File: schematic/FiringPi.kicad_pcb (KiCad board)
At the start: 4 copper layers, 65 x 85.9 mm, 72 parts, among them IC1 HX711, J12 UART, P1 Raspberry Pi GPIO Header, Q1 MMBT4403, U4 LM2596S-5, U5 ADS1115IDGS, U6 MAX31865xAP, U7 MAX31865xAP

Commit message: Updated silkscreen labels
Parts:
- renumbered RELAY1 to RELAY, J12 to UART
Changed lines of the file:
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@@
     (property "Sheetname" "")
     (attr through_hole)
-    (fp_text reference "J12" (at 9.5 -0.025 270 unlocked) (layer "F.SilkS")
+    (fp_text reference "UART" (at 9.5 -0.025 270 unlocked) (layer "F.SilkS")
       (effects (font (size 1 1) (thickness 0.15)))
     )
@@
     (property "Sheetname" "")
     (attr through_hole)
-    (fp_text reference "RELAY1" (at 3 11.425) (layer "F.SilkS")
-      (effects (font (size 1 1) (thickness 0.15)))
-    )
+    (fp_text reference "RELAY" (at 3 11.425) (layer "F.SilkS")
+      (effects (font (size 1 1) (thickness 0.15)))
+    )

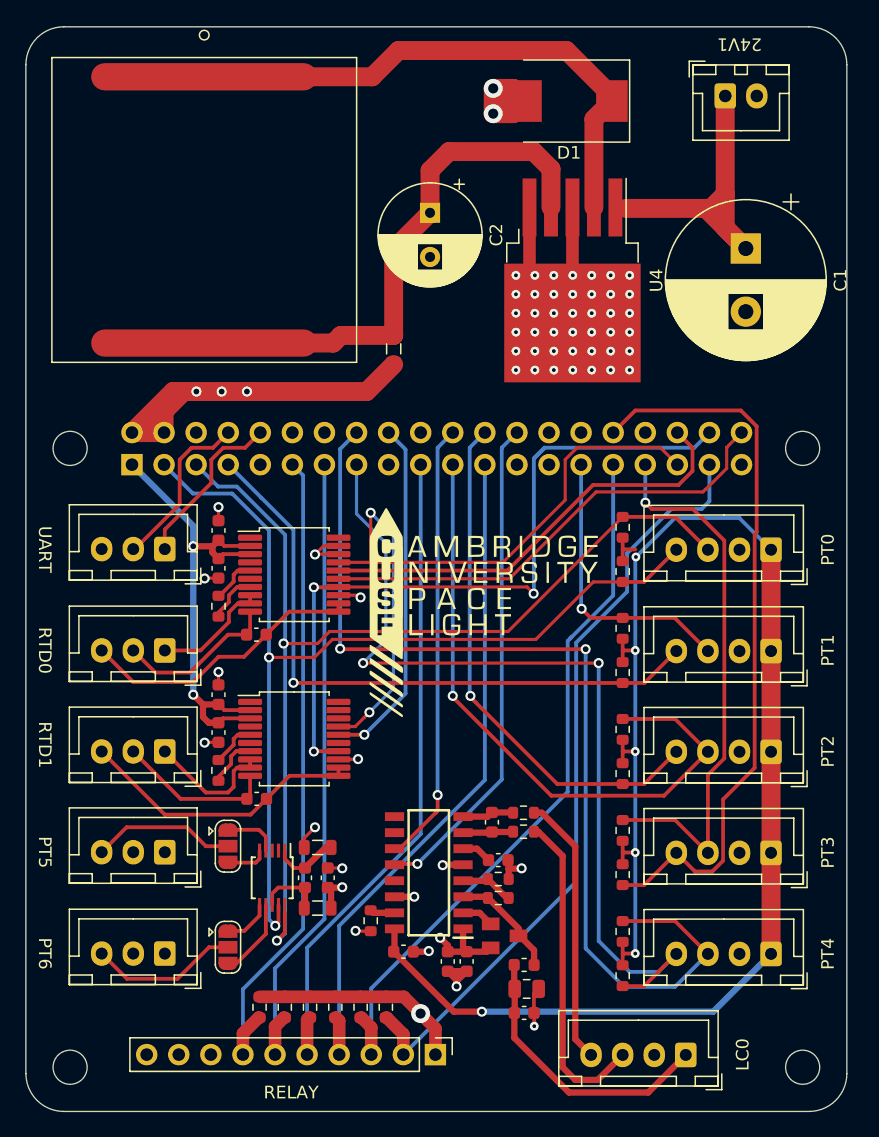
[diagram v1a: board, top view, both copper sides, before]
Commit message: Fixed DRC errors
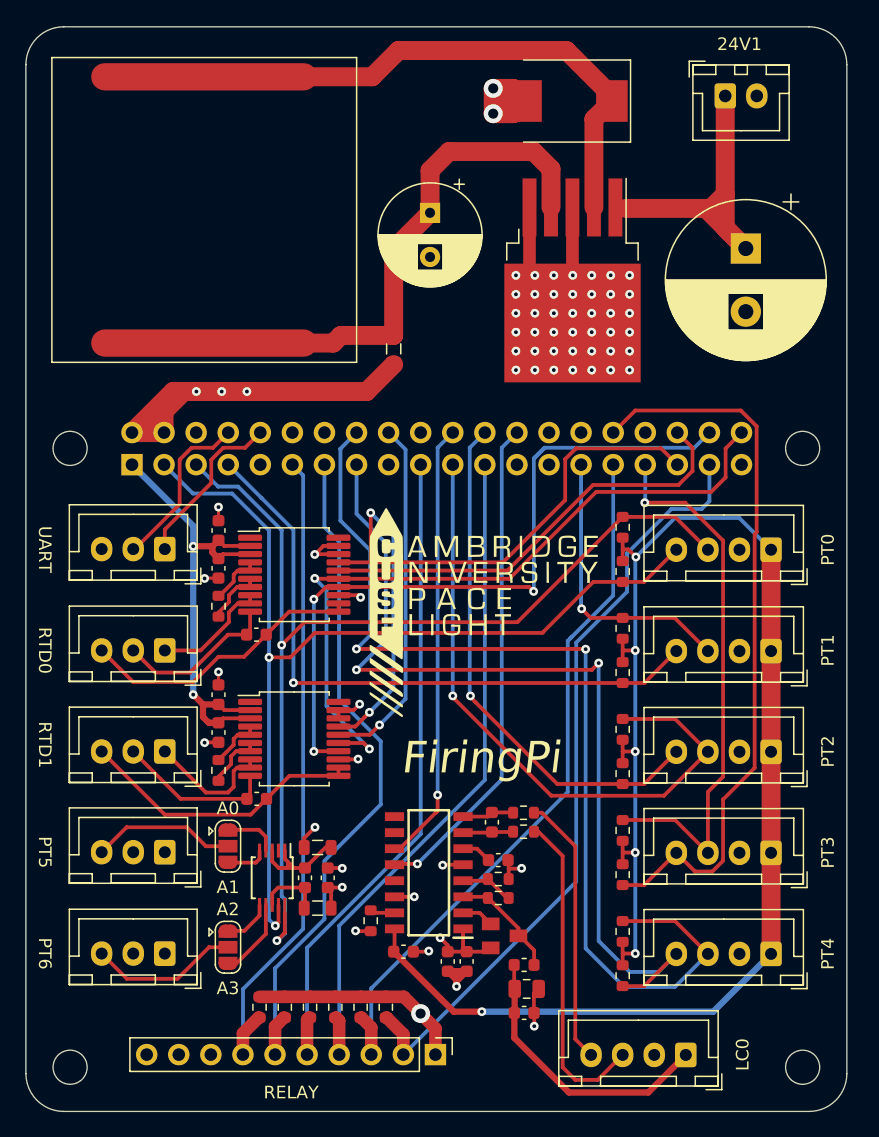
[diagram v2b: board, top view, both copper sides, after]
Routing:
- net SCL5: track 0.00 -> 43.5 mm, vias 0 -> 1
- net +3.3V: track 242.1 -> 202.8 mm, vias 9 -> 8
- net SCLK: track 37.7 -> 57.9 mm, vias 0 -> 2
- net RLY4: track 51.6 -> 55.3 mm
- net Net-(C10-Pad2): track 5.29 -> 8.85 mm
- net GND: track 72.1 -> 74.6 mm, vias 60 -> 61
- net SDA6: track 71.1 -> 72.6 mm
- net RLY0: track 63.0 -> 61.7 mm
- net MOSI: track 59.2 -> 58.4 mm
- net Net-(R16-Pad1): track 3.60 -> 4.25 mm
- net Net-(R15-Pad2): track 3.98 -> 4.63 mm
- net Net-(R15-Pad1): track 3.65 -> 4.30 mm
- net Net-(R16-Pad2): track 4.03 -> 4.68 mm
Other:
- board text added: "A0"
- board text added: "A1"
- board text added: "A2"
- board text added: "A3"
- board text added: "FiringPi"

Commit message: Small tweaks
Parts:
- added D2: LED_Small, LED_SMD:LED_0805_2012Metric, F.Cu at (54.9, 33.9)
- added R1: 330, Resistor_SMD:R_0603_1608Metric, F.Cu at (54.9, 35.8)
- moved C2 7.15 mm to (56.5, 44.5), turned to 90 degrees
- moved D1 5.83 mm to (61.7, 28.4)
- moved FB1 1.13 mm to (53.6, 49.2)
- moved U4 1.05 mm to (67.7, 41.6)
- renumbered UART to J12, RELAY to RELAY1
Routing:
- net Net-(D1-Pad1): track 44.0 -> 39.5 mm
- net Net-(R1-Pad1): track 43.3 -> 47.5 mm
- net Net-(D2-Pad2): track 0.00 -> 1.95 mm
- net GND: track 74.6 -> 75.8 mm, vias 61 -> 62
- added copper zone on F.Cu, net +24V
- added copper zone on F.Cu, net +5V
- added copper zone on F.Cu, net Net-(D1-Pad1)
- added copper zone on F.Cu, net Net-(R1-Pad1)
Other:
- board text added: "+"
- board text added: "-"
- board text added: "24V"
- board text added: "RELAY"
- board text added: "UART"

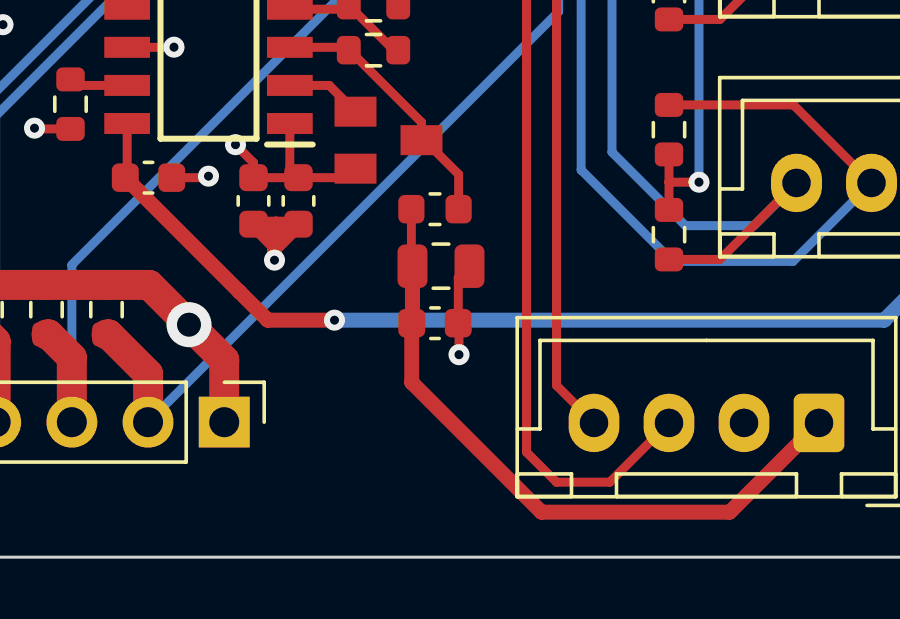
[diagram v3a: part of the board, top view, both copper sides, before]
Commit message: Added BOM & part Nos
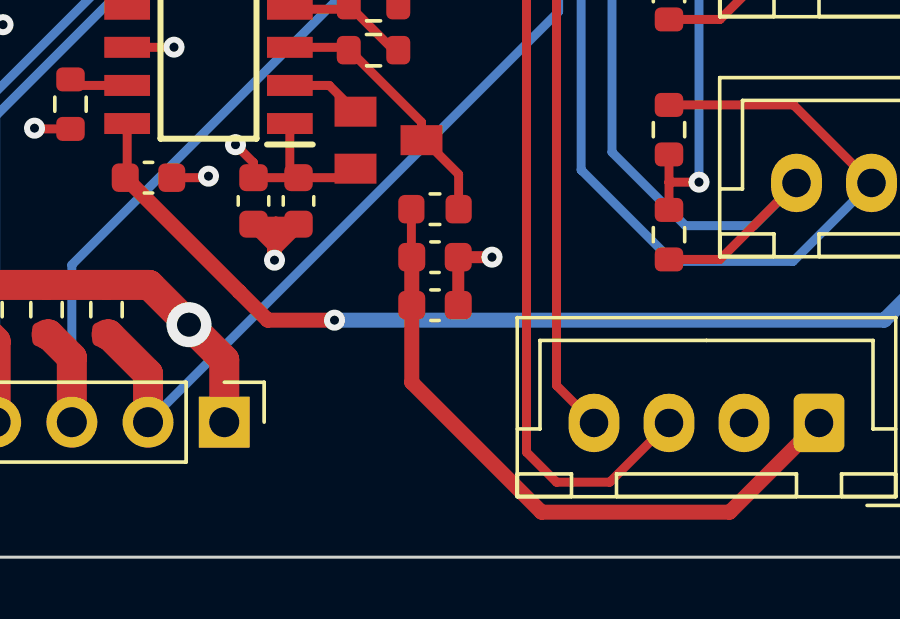
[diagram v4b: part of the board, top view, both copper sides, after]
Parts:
- C4: footprint Capacitor_SMD:C_0805_2012Metric -> Capacitor_SMD:C_0603_1608Metric
- R12: value 20k -> 430
- R15, R16: value 400R -> 430R
- moved C3 0.60 mm to (64.0, 100.1)
- moved C4 0.36 mm to (64.0, 98.5)

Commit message: Generated gerbers
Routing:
- net Net-(C2-Pad1): track 47.5 -> 46.1 mm
- net Net-(D1-Pad1): track 39.5 -> 38.4 mm
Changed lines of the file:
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@@
   (via (at 39.75 60.65) (size 0.7) (drill 0.3) (layers "F.Cu" "B.Cu") (net 2))
   (segment (start 63.175 102.675) (end 63.175 100.1) (width 0.5) (layer "F.Cu") (net 3))
-  (segment (start 63.1625 96.9) (end 63.1625 98.7625) (width 0.3) (layer "F.Cu") (net 3))
-  (segment (start 63.175 100.1) (end 63.175 98.5) (width 0.5) (layer "F.Cu") (net 3))
+  (segment (start 63.175 98.5) (end 63.175 100.1) (width 0.4) (layer "F.Cu") (net 3))
   (segment (start 67.5 107) (end 73.775 107) (width 0.5) (layer "F.Cu") (net 3))
-  (segment (start 63.1625 98.7625) (end 63.2 98.8) (width 0.3) (layer "F.Cu") (net 3))
+  (segment (start 63.1625 96.9) (end 63.1625 98.4875) (width 0.4) (layer "F.Cu") (net 3))
   (segment (start 63.175 102.675) (end 67.5 107) (width 0.5) (layer "F.Cu") (net 3))
   (segment (start 73.775 107) (end 76.75 104.025) (width 0.5) (layer "F.Cu") (net 3))
@@
   (segment (start 61.625 24.5) (end 54 24.5) (width 1.5) (layer "F.Cu") (net 13))
   (segment (start 69.475 32.825) (end 65.075 28.425) (width 1.5) (layer "F.Cu") (net 13))
+  (segment (start 69.475 32.825) (end 69.475 35.825) (width 1.5) (layer "F.Cu") (net 13))
   (segment (start 51.91968 26.58032) (end 38.62132 26.58032) (width 1.5) (layer "F.Cu") (net 13))
-  (segment (start 69.475 36.925) (end 69.475 32.825) (width 1.5) (layer "F.Cu") (net 13))
   (segment (start 54 24.5) (end 51.91968 26.58032) (width 1.5) (layer "F.Cu") (net 13))
   (segment (start 60.425 92.775) (end 61.3 93.65) (width 0.3) (layer "F.Cu") (net 14))
@@
   (segment (start 55.725 35.8) (end 58.7 35.8) (width 0.4) (layer "F.Cu") (net 73))
   (segment (start 64.75 31.75) (end 62.75 31.75) (width 1.5) (layer "F.Cu") (net 73))
-  (segment (start 66.025 35.875) (end 66.025 33.025) (width 1.5) (layer "F.Cu") (net 73))
   (segment (start 66.025 33.025) (end 64.75 31.75) (width 1.5) (layer "F.Cu") (net 73))
   (segment (start 59.25 42.25) (end 57 44.5) (width 1.5) (layer "F.Cu") (net 73))
+  (segment (start 66.025 33.025) (end 66.025 35.875) (width 1.5) (layer "F.Cu") (net 73))
   (segment (start 53.09614 47.66232) (end 53.62132 48.1875) (width 1.5) (layer "F.Cu") (net 73))
   (segment (start 58.7 35.8) (end 59.25 35.25) (width 0.4) (layer "F.Cu") (net 73))
   (segment (start 57 44.5) (end 56.5 44.5) (width 1.5) (layer "F.Cu") (net 73))
-  (segment (start 66.025 35.875) (end 66.025 37.225) (width 1.5) (layer "F.Cu") (net 73))
   (segment (start 53.62132 47.37868) (end 56.5 44.5) (width 1.5) (layer "F.Cu") (net 73))
   (segment (start 53.62132 48.1875) (end 53.62132 47.37868) (width 1.5) (layer "F.Cu") (net 73))
@@
     (polygon
       (pts
-        (xy 70.25 33.25)
+        (xy 70 33.25)
         (xy 68.5 33.25)
         (xy 66 30.75)
@@
         (xy 28.65 31)
         (xy 28.65 22.5)
-        (xy 70.15 22.5)
+        (xy 70 22.5)
       )
     )
